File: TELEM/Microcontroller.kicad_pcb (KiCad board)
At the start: 4 copper layers, 77.4 x 80.1 mm, 31 parts, among them J3 Conn_01x02, J4 Conn_01x02_Pin, M3 MountingHole, M3_1 MountingHole, U2 ESP32-DEVKIT-C, U3 TJA1050T/CM,118, U4 TPS54560BQDDARQ1

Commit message: updated Julias IMU to use the revised buck converter and connectors. made the back plane mostly a ground plane (for the buck converter)
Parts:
- renumbered J3 to J1, U4 to U1, U1 to U6

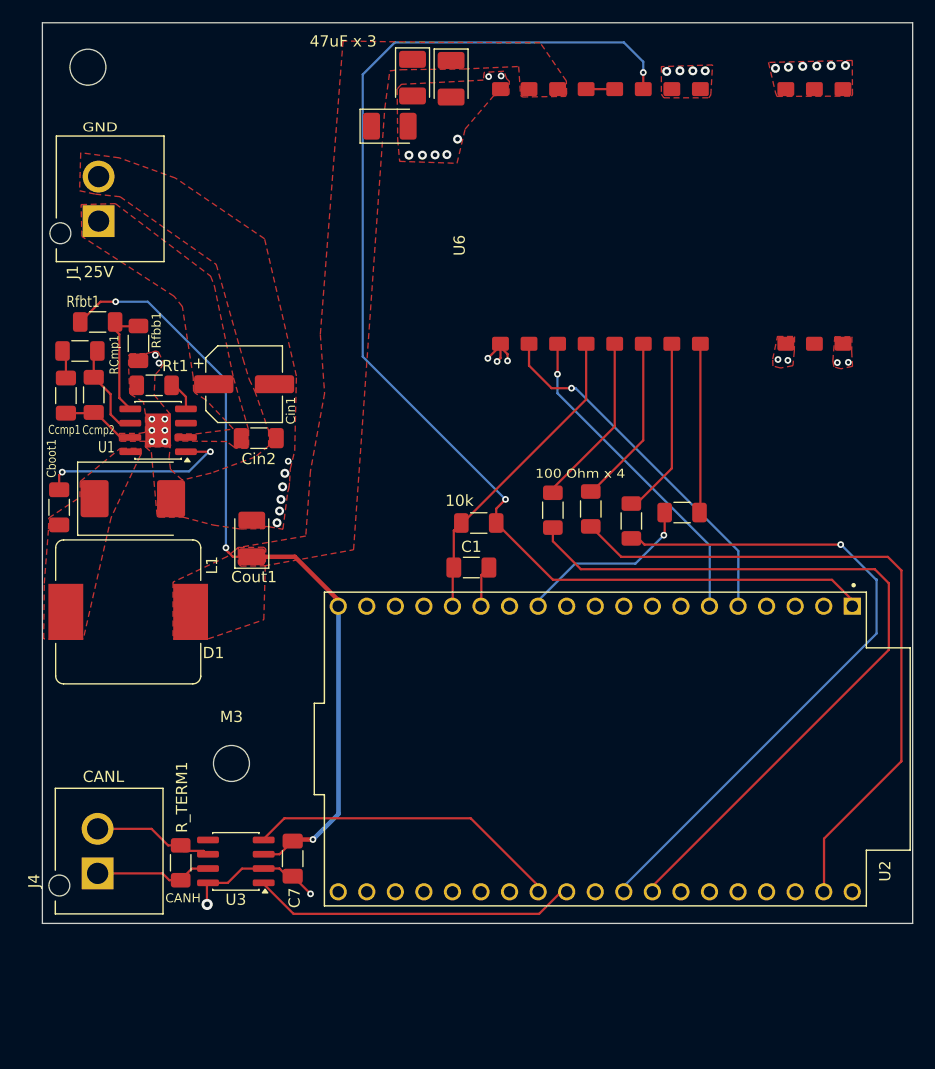
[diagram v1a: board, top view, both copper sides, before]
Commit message: small updates to buck, fixed vias, and remove connection to input connector ground pad
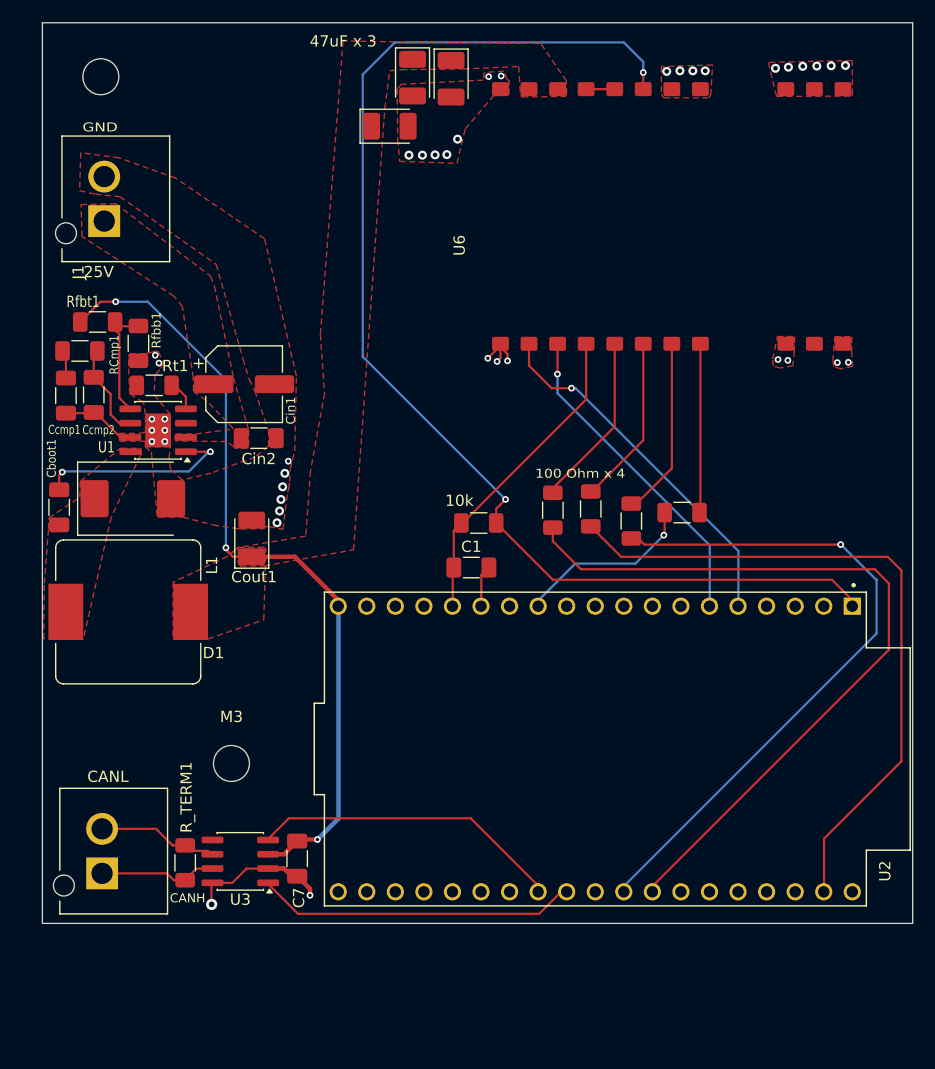
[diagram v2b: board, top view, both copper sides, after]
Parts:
- moved M3_1 1.43 mm to (44.8, 40.8)
- moved J1 0.50 mm to (46.1, 51.7)
- moved C7 0.40 mm to (62.3, 110.3)
- moved J4 0.40 mm to (45.9, 109.7)
- moved R_TERM1 0.40 mm to (52.3, 110.7)
- moved U3 0.40 mm to (57.2, 110.6)

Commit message: PDB_Schematic mostly updated
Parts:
- added M4: MountingHole, MountingHole:MountingHole_3.2mm_M3, F.Cu at (112.8, 122.0)
- moved J4 58.2 mm to (103.1, 120.5), turned to 180 degrees
- moved R_TERM1 44.7 mm to (95.8, 121.2), turned to -90 degrees
- moved U3 34.7 mm to (90.4, 120.7), turned to 0 degrees
- moved C7 25.4 mm to (85.4, 120.8), turned to -90 degrees
- moved M3 24.3 mm to (44.0, 122.8)
- moved Cboot1 23.4 mm to (41.1, 102.5)
- moved Ccmp1 23.4 mm to (41.7, 92.5)
- moved Ccmp2 23.4 mm to (44.1, 92.5)
- moved Cin1 23.4 mm to (57.5, 91.5)
- moved Cin2 23.4 mm to (58.8, 96.3)
- moved Cout1 23.4 mm to (58.2, 105.2)
- moved D1 23.4 mm to (47.6, 101.7)
- moved J1 23.4 mm to (46.1, 75.0)
- moved L1 23.4 mm to (47.2, 111.8)
- moved RCmp1 23.4 mm to (42.9, 88.6)
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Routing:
- net 5.2V_OUT: track 70.3 -> 45.3 mm, vias 3 -> 29
- net Net-(U2-IO17): track 28.8 -> 6.24 mm
- net Net-(U2-IO16): track 27.4 -> 19.4 mm
- net /CANH: track 10.6 -> 16.8 mm
- net GND: track 25.0 -> 20.2 mm, vias 40 -> 144
- net Net-(U1-SW): track 0.00 -> 1.77 mm
- net Net-(U1-BOOT): track 17.8 -> 16.7 mm
- net /CANL: track 10.8 -> 9.78 mm
- net Net-(J1-Pin_1): track 0.87 -> 0.00 mm
- added copper zone on In2.Cu, net 5.2V_OUT
- added copper zone on B.Cu, net GND
- removed copper zone on In2.Cu, net GND
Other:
- board size 77.4 x 80.1 mm -> 77.4 x 90.5 mm
- board text added: "M3"
- board text added: "R_TERM"

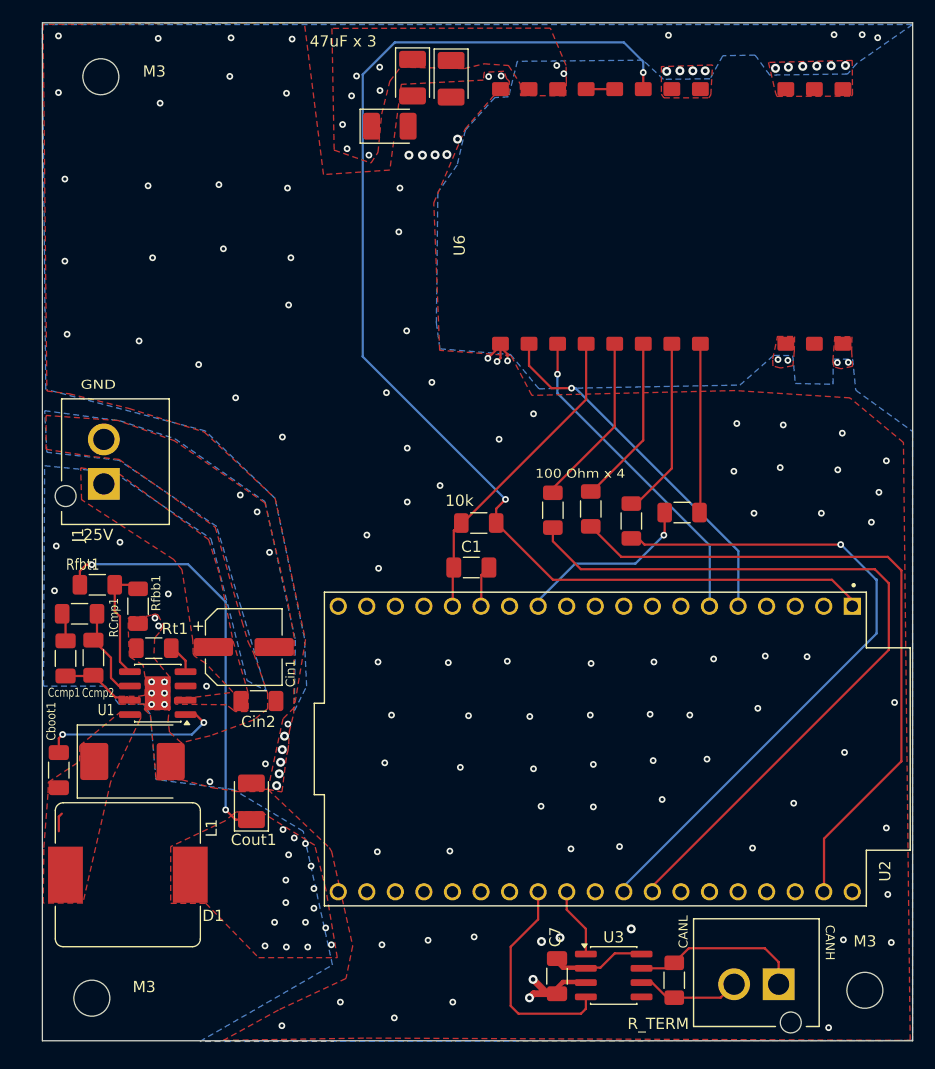
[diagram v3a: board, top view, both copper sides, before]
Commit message: sry forgot to push, waiting on PCB shipping atm. Notes: split power distribution into two boards, one for the main 25V distribution, and another for 12V stuff. Also updated CAN transciever. the previous one was a 5V logic one (same logic as its power), and would have fried our ESPs data pins
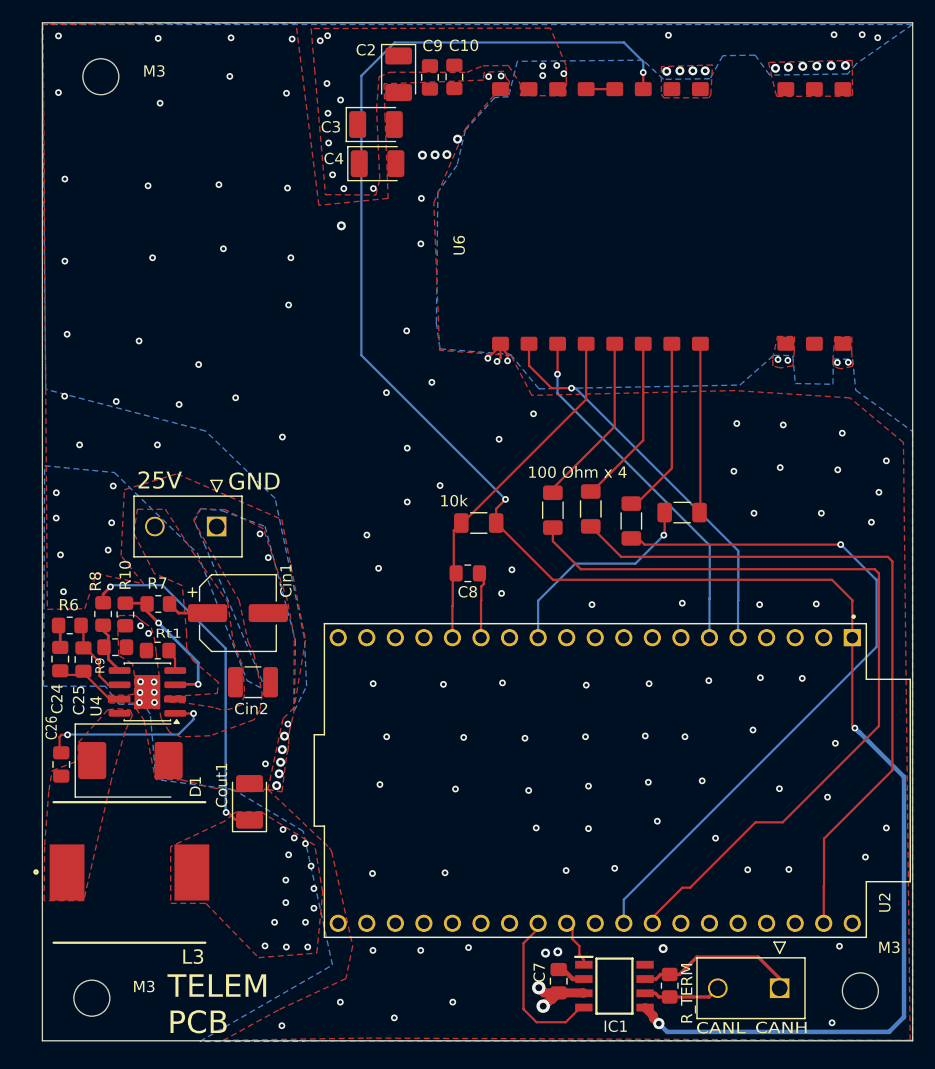
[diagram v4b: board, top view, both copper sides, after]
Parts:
- removed C1, Cboot1: 100nF, Capacitor_SMD:C_1206_3216Metric_Pad1.33x1.80mm_HandSolder
- removed Ccmp1: 10nF, Capacitor_SMD:C_1206_3216Metric_Pad1.33x1.80mm_HandSolder
- removed Ccmp2: 10pF, Capacitor_SMD:C_1206_3216Metric_Pad1.33x1.80mm_HandSolder
- removed J1: Conn_01x02, PROVE-footprints:TE_1877285-2
- removed J4: Conn_01x02_Pin, PROVE-footprints:TE_1877285-2
- removed L1: 22uH, Inductor_SMD:L_Bourns_SRP1245A
- removed RCmp1: 18.2kOhm, Resistor_SMD:R_1206_3216Metric_Pad1.30x1.75mm_HandSolder
- removed Rfbb1: 11.8kOhm, Resistor_SMD:R_1206_3216Metric_Pad1.30x1.75mm_HandSolder
- removed Rfbt1: 64.9kOhm, Resistor_SMD:R_1206_3216Metric_Pad1.30x1.75mm_HandSolder
- removed U1: TPS54560BQDDARQ1, Package_SO:SOIC-8-1EP_3.9x4.9mm_P1.27mm_EP2.29x3mm
- removed U3: TJA1050T/CM,118, Package_SO:SOIC-8_3.9x4.9mm_P1.27mm
- added C10: 100nF, Capacitor_SMD:C_0805_2012Metric_Pad1.18x1.45mm_HandSolder, F.Cu at (76.2, 40.8)
- added C24: 10nF, Capacitor_SMD:C_0805_2012Metric_Pad1.18x1.45mm_HandSolder, F.Cu at (41.2, 92.6)
- added C25: 10pF, Capacitor_SMD:C_0805_2012Metric_Pad1.18x1.45mm_HandSolder, F.Cu at (43.2, 92.6)
- added C26: 100nF, Capacitor_SMD:C_0805_2012Metric_Pad1.18x1.45mm_HandSolder, F.Cu at (41.3, 102.0)
- added C8: 100nF, Capacitor_SMD:C_0805_2012Metric_Pad1.18x1.45mm_HandSolder, F.Cu at (77.4, 85.0)
- added C9: 100nF, Capacitor_SMD:C_0805_2012Metric_Pad1.18x1.45mm_HandSolder, F.Cu at (74.1, 40.9)
- added IC1: TJA1044BT/0Z, PROVE-footprints:SOIC127P600X175-8N, F.Cu at (90.5, 121.7)
- added J2: 39-28-1023, PROVE-footprints:39-28-1023, F.Cu at (105.2, 121.9)
- added J24: 39-28-1023, PROVE-footprints:39-28-1023, F.Cu at (55.1, 80.8)
- added L3: SRP1265A-220M, PROVE-footprints:SRP1265A, F.Cu at (47.3, 111.6)
- added R10: 38.3k, Resistor_SMD:R_0805_2012Metric_Pad1.20x1.40mm_HandSolder, F.Cu at (47.0, 88.6)
- added R6: 18.2k, Resistor_SMD:R_0805_2012Metric_Pad1.20x1.40mm_HandSolder, F.Cu at (42.0, 89.6)
- added R7: 590k, Resistor_SMD:R_0805_2012Metric_Pad1.20x1.40mm_HandSolder, F.Cu at (49.9, 87.7)
- added R8: 64.9kOhm, Resistor_SMD:R_0805_2012Metric_Pad1.20x1.40mm_HandSolder, F.Cu at (45.0, 88.6)
- added R9: 11.8kOhm, Resistor_SMD:R_0805_2012Metric_Pad1.20x1.40mm_HandSolder, F.Cu at (46.1, 91.5)
- added U4: TPS54560BQDDARQ1, Package_SO:SOIC-8-1EP_3.9x4.9mm_P1.27mm_EP2.29x3mm, F.Cu at (48.9, 95.5)
- C7: value 0.1u -> 100nF; footprint Capacitor_SMD:C_1206_3216Metric_Pad1.33x1.80mm_HandSolder -> Capacitor_SMD:C_0805_2012Metric_Pad1.18x1.45mm_HandSolder
- Cin2: footprint Capacitor_SMD:C_1206_3216Metric_Pad1.33x1.80mm_HandSolder -> Capacitor_SMD:C_1210_3225Metric_Pad1.33x2.70mm_HandSolder
- R_TERM1, Rt1: footprint Resistor_SMD:R_1206_3216Metric_Pad1.30x1.75mm_HandSolder -> Resistor_SMD:R_0805_2012Metric_Pad1.20x1.40mm_HandSolder
- moved C4 8.26 mm to (69.4, 48.5), turned to 0 degrees
- moved C2 4.69 mm to (71.3, 40.6)
- moved Cin1 3.06 mm to (57.0, 88.5)
- moved U2 2.80 mm to (88.8, 103.4)
- moved Cin2 1.74 mm to (58.3, 94.7)
- moved C3 1.24 mm to (69.3, 45.0)
- moved R_TERM1 0.63 mm to (95.4, 121.6)
- moved C7 0.47 mm to (85.5, 121.2), turned to 90 degrees
- moved Rt1 0.41 mm to (49.9, 91.8)
- moved M4 0.40 mm to (112.3, 122.1)
- moved D1 0.20 mm to (47.4, 101.6)
- moved Cout1 0.18 mm to (58.0, 105.3)
- renumbered R7 to R3
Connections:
- net Net-(J1-Pin_1) renamed /buck/25V_IN
- net Net-(U2-3V3) renamed /3v3
- C7 pad 1: GND -> 5.2V_OUT
- C7 pad 2: 5.2V_OUT -> GND
- U2 pad 14: Net-(U2-GND1) -> GND
- U2 pad 38: unconnected-(U2-GND3-Pad38) -> GND
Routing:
- net /3v3: track 110.0 -> 173.2 mm, vias 2 -> 4
- net Net-(U1-BOOT): track 16.7 -> 0.00 mm, vias 2 -> 0
- net Net-(U4-BOOT): track 0.00 -> 16.0 mm, vias 0 -> 2
- net Net-(U4-EN): track 0.00 -> 13.0 mm, vias 0 -> 2
- net Net-(U1-FB): track 10.5 -> 0.00 mm
- net Net-(U1-COMP): track 8.47 -> 0.00 mm
- net 5.2V_OUT: track 45.3 -> 37.7 mm, vias 29 -> 31
- net Net-(U4-COMP): track 0.00 -> 7.24 mm
- net Net-(IC1-RXD): track 19.4 -> 14.1 mm
- net Net-(U4-FB): track 0.00 -> 4.66 mm
- net Net-(U2-IO19): track 68.8 -> 72.7 mm
- net Net-(U2-GND1): track 3.73 -> 0.00 mm
- net /buck/25V_IN: track 0.00 -> 3.71 mm
- net Net-(U2-IO34): track 32.3 -> 35.1 mm
- net Net-(U2-IO14): track 16.1 -> 18.9 mm
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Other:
- board text added: "TELEM PCB"
- board text removed: "47uF x 3"
